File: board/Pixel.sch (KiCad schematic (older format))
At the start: 31 parts, among them J0 Batt+, J1 Batt-, SW0 Reset, SW1 Up, SW2 Down, SW3 Left, SW4 Right, SW5 BTN A, SW6 BTN B, SW7 BTN C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

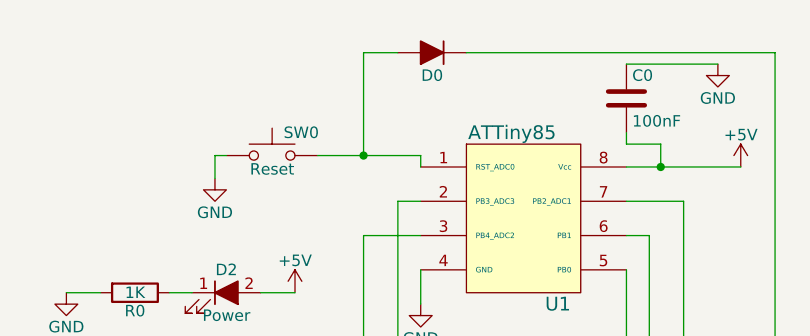
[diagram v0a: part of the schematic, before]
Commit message: rotated reset diode
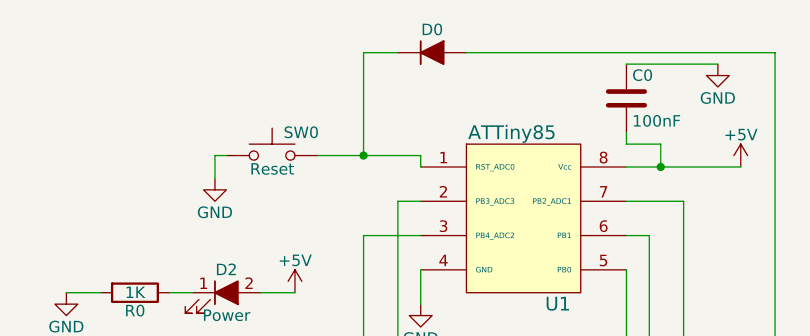
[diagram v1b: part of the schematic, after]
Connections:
- net at SW0.2, U1.1 (RST_ADC0): now also D0.1 (K); no longer D0.2 (A)
- net at C1.1, D1.2 (A), R10.2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: now also D0.2 (A); no longer D0.1 (K)
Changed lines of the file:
@@
 F 3 "" H 3400 850 50  0001 C CNN
 	1    3400 850
-	-1   0    0    1
+	1    0    0    -1
 $EndComp
 $Comp
@@
 Connection ~ 3100 1300
 Wire Wire Line
-	3550 850  4900 850
-Wire Wire Line
-	3250 850  3100 850
-Wire Wire Line
 	3100 850  3100 1300
 Wire Wire Line
@@
 Wire Wire Line
 	2550 2200 1000 2200
+Wire Wire Line
+	3100 850  3250 850
+Wire Wire Line
+	3550 850  4900 850
 $EndSCHEMATC
